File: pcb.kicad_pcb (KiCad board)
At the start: 2 copper layers, 247.4 x 96.5 mm, 228 parts, among them J0 USB_mini_micro_B, P1 CONN_3X2, P2 CONN_4, SW1.1 Backtick, SW1.10 9, SW1.11 0, SW1.12 -, SW1.13 =, SW1.2 1, SW1.3 2, SW1.4 3, SW1.5 4, SW1.6 5, SW1.7 6, SW1.8 7, SW1.9 8, SW2A1 Tab, SW2A10 I, SW2A11 O, SW2A12 P, SW2A13 /, SW2A2 Q, SW2A3 W, SW2A4 E, SW2A5 R, SW2A6 T, SW2A8 Y, SW2A9 U, SW2B1 Tab, SW2B10 I, SW2B11 O, SW2B12 P, SW2B13 /, SW2B2 Q, SW2B3 W, SW2B4 E, SW2B5 R, SW2B6 T, SW2B7 Y, SW2B8 Y, SW2B9 U, SW3A1 Bksp, SW3A10 K, SW3A11 L, SW3A12 ;, SW3A13 Enter, SW3A2 A, SW3A3 S, SW3A4 D, SW3A5 F, SW3A6 G, SW3A8 H, SW3A9 J, SW3B1 Bksp, SW3B10 K, SW3B11 L, SW3B12 ;, SW3B13 Enter, SW3B2 A, SW3B3 S, SW3B4 D, SW3B5 F, SW3B6 G, SW3B7 H, SW3B8 H, SW3B9 J, SW4A1 LShift, SW4A10 ,, SW4A11 ., SW4A13 RShift, SW4A3 Z, SW4A4 X, SW4A5 C, SW4A6 V, SW4A8 N, SW4A9 M, SW4B1 LShift, SW4B10 ,, SW4B11 ., SW4B12 .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

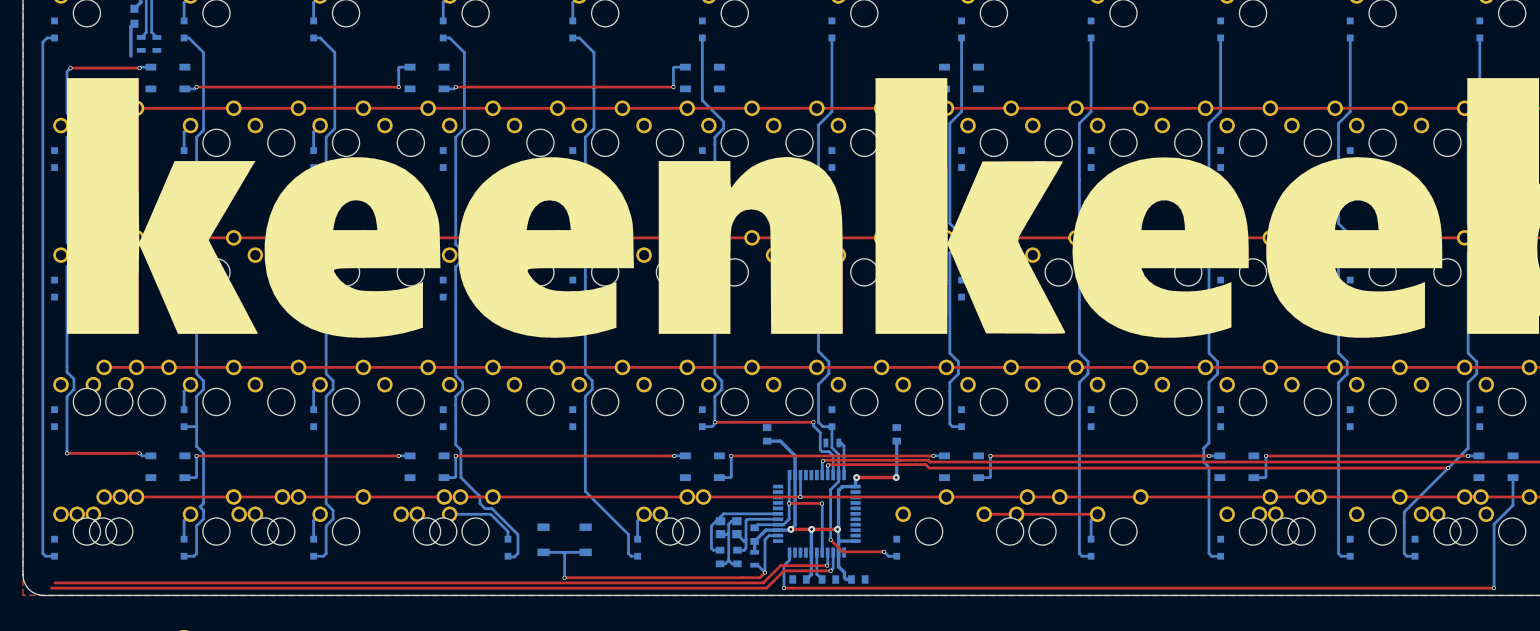
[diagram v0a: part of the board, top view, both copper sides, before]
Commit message: About half of rows/columns connected to microcontroller.
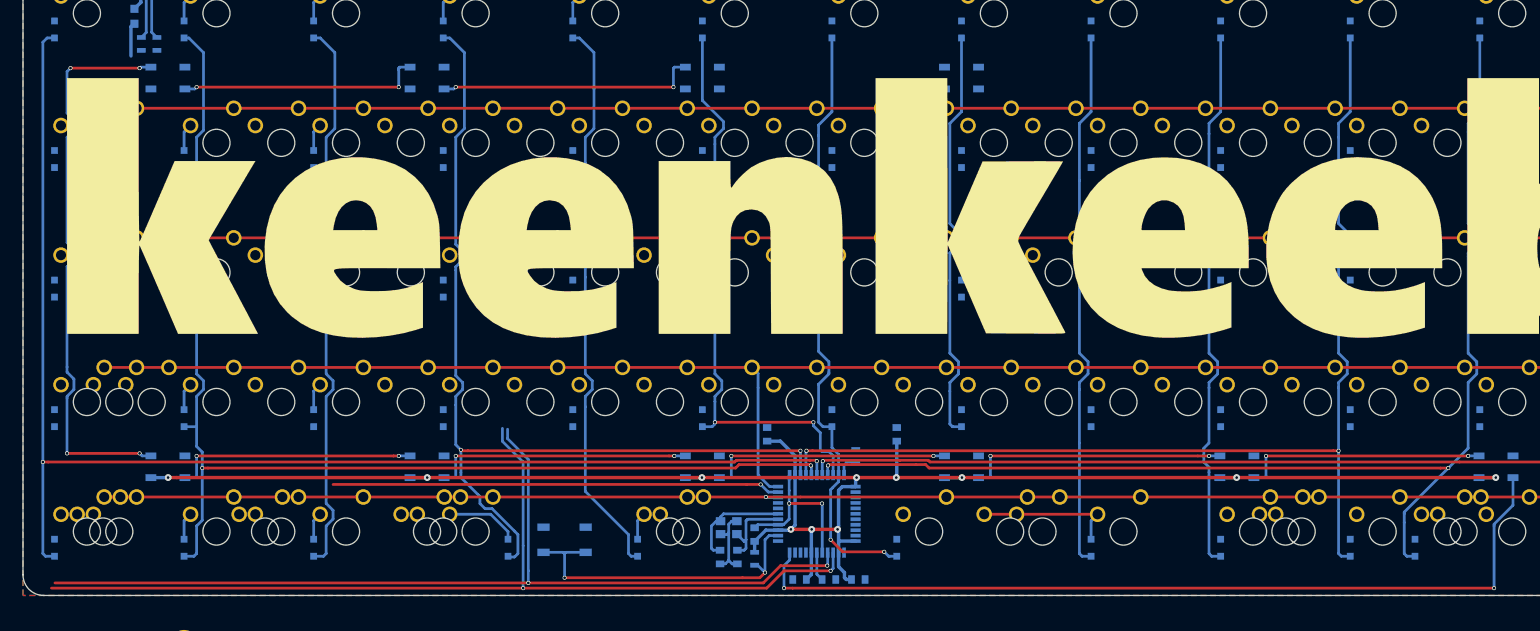
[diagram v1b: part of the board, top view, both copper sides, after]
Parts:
- moved G3 301.4 mm to (321.8, 138.8), turned to 270 degrees
- moved G2 288.6 mm to (319.0, 129.4), turned to 270 degrees
- moved R4 3.92 mm to (198.8, 165.1), turned to 270 degrees
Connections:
- U1 pad 1: /matrix/Col2 -> Net-(U1-Pad1)
- U1 pad 20: Net-(U1-Pad20) -> /matrix/Row5
- U1 pad 21: /matrix/Col11 -> Net-(U1-Pad21)
- U1 pad 22: /matrix/Col9 -> /matrix/Row4
- U1 pad 25: /matrix/Row5 -> /matrix/Col4
- U1 pad 26: Net-(U1-Pad26) -> /matrix/Col11
- U1 pad 27: Net-(U1-Pad27) -> /matrix/Col2
- U1 pad 28: Net-(U1-Pad28) -> /matrix/Col1
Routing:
- net VCC: track 75.7 -> 280.0 mm, vias 5 -> 11
- net /matrix/Col1: track 79.0 -> 195.0 mm, vias 0 -> 2
- net /matrix/Col2: track 88.3 -> 178.9 mm, vias 0 -> 2
- net /matrix/Col11: track 80.5 -> 162.3 mm, vias 0 -> 2
- net Net-(U1-Pad21): track 0.00 -> 65.9 mm, vias 0 -> 1
- net /matrix/Col4: track 86.0 -> 139.5 mm, vias 0 -> 2
- net Net-(R1-Pad1): track 118.4 -> 143.2 mm, vias 1 -> 2
- net Net-(R2-Pad1): track 116.5 -> 140.4 mm, vias 1 -> 2
- net /matrix/Row4: track 228.6 -> 248.4 mm
- net Net-(R4-Pad2): track 5.22 -> 3.35 mm
- net /matrix/Row5: track 231.8 -> 230.4 mm

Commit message: Focusing efforts on one main layout (semi-ortho), so that PCB-mounted and Alps components can be supported
Updated keenkeeb-reb1.png with new layout.
Started removing footprints and adding new spacebar footprints.
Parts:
- removed SW2B1: Tab, footprints:MX_100_Plate
- removed SW2B10: I, footprints:MX_100_Plate
- removed SW2B11: O, footprints:MX_100_Plate
- removed SW2B12: P, footprints:MX_100_Plate
- removed SW2B13: /, footprints:MX_100_Plate
- removed SW2B2: Q, footprints:MX_100_Plate
- removed SW2B3: W, footprints:MX_100_Plate
- removed SW2B4: E, footprints:MX_100_Plate
- removed SW2B5: R, footprints:MX_100_Plate
- removed SW2B6: T, footprints:MX_100_Plate
- removed SW2B7, SW2B8: Y, footprints:MX_100_Plate
- removed SW2B9: U, footprints:MX_100_Plate
- removed SW3B1: Bksp, footprints:MX_100_Plate
- removed SW3B10: K, footprints:MX_100_Plate
- removed SW3B11: L, footprints:MX_100_Plate
- removed SW3B12: ;, footprints:MX_100_Plate
- removed SW3B13: Enter, footprints:MX_100_Plate
- removed SW3B2: A, footprints:MX_100_Plate
- removed SW3B3: S, footprints:MX_100_Plate
- removed SW3B4: D, footprints:MX_100_Plate
- removed SW3B5: F, footprints:MX_100_Plate
- removed SW3B6: G, footprints:MX_100_Plate
- removed SW3B7, SW3B8: H, footprints:MX_100_Plate
- removed SW3B9: J, footprints:MX_100_Plate
- removed SW4B1: LShift, footprints:MX_150_Plate
- removed SW4B10: ,, footprints:MX_100_Plate
- removed SW4B11, SW4B12: ., footprints:MX_100_Plate
- removed SW4B13: RShift, footprints:MX_150_Plate
- removed SW4B2, SW4B3: Z, footprints:MX_100_Plate
- removed SW4B4: X, footprints:MX_100_Plate
- removed SW4B5: C, footprints:MX_100_Plate
- removed SW4B6: V, footprints:MX_100_Plate
- removed SW4B8: N, footprints:MX_100_Plate
- removed SW4B9: M, footprints:MX_100_Plate
- removed SW5B1: LCtrl, footprints:MX_125_Plate
- removed SW5B10, SW5B12, SW5B13: 1.25, footprints:MX_125_Plate
- removed SW5B2: LGUI, footprints:MX_125_Plate
- removed SW5B4: LAlt, footprints:MX_125_Plate
- added LED11: WS2812b, LEDs:LED_WS2812B-PLCC4, B.Cu at (254.8, 109.5)
- added LED12: WS2812b, LEDs:LED_WS2812B-PLCC4, B.Cu at (292.9, 109.5)
- added SW5B7: 2.75, footprints:MX_275_Plate_NoStabHoles, F.Cu at (178.6, 176.2)
- added SW5C9: 1.5, footprints:MX_150_Plate, F.Cu at (233.4, 176.2)
- added SW5D7: 1, footprints:MX_100_Plate, F.Cu at (161.9, 176.2)
- SW5A7: renamed from SW5A5; value Fn -> 2.25
- SW5A9: value Space -> 2.75
- SW5B9: value Space -> 2.25; footprint footprints:MX_275_Plate_NoStabHoles -> footprints:MX_225_Plate_NoStabHoles
- SW5C5: value Fn -> 1.5; footprint footprints:MX_200_Plate_NoStabHoles -> footprints:MX_150_Plate
- SW5C7: value Fn -> 2/3
- moved C1 128.3 mm to (90.2, 109.1), turned to 90 degrees
- moved C8 126.3 mm to (83.1, 128.1), turned to 180 degrees
- moved R3 118.8 mm to (79.2, 124.1)
- moved C7 103.6 mm to (88.4, 126.4), turned to 180 degrees
- moved U1 101.2 mm to (102.4, 128.6), turned to 270 degrees
- moved C5 101.0 mm to (110.0, 122.3)
- moved PB0 99.6 mm to (59.5, 152.4)
- moved C4 98.5 mm to (120.7, 123.8)
- moved C6 84.9 mm to (106.9, 140.8), turned to 270 degrees
- moved OSC0 81.6 mm to (114.0, 127.6), turned to 315 degrees
- moved C2 78.7 mm to (123.7, 126.4), turned to 0 degrees
- moved C3 75.1 mm to (123.7, 128.9), turned to 0 degrees
- moved D2.3 19.2 mm to (138.1, 119.1)
- moved D3.3 19.2 mm to (138.1, 138.1)
- moved D2.2 19.2 mm to (119.1, 119.1)
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- renumbered SW4B7 to SW4.7, SW5C9 to SW5D9
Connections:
- D5.5 pad 2: /matrix/Col5 -> Net-(D5.5-Pad2)
- SW5A4 pad 1: /matrix/Row5 -> Net-(D5.4-Pad1)
- SW5A4 pad 2: Net-(D5.4-Pad1) -> /matrix/Row5
- SW5A7 pad 1: /matrix/Row5 -> Net-(D5.7-Pad1)
- SW5A7 pad 2: Net-(D5.5-Pad1) -> /matrix/Row5
- SW5B9 pad 1: /matrix/Row5 -> Net-(D5.9-Pad1)
- SW5B9 pad 2: Net-(D5.9-Pad1) -> /matrix/Row5
- SW5D9 pad 1: /matrix/Row5 -> Net-(D5.9-Pad1)
- SW5D9 pad 2: Net-(D5.9-Pad1) -> /matrix/Row5
- U1 pad 20: /matrix/Row5 -> /matrix/Col13
- U1 pad 21: Net-(U1-Pad21) -> /matrix/Col12
- U1 pad 22: /matrix/Row4 -> /matrix/Col11
- U1 pad 25: /matrix/Col4 -> /matrix/Col10
- U1 pad 26: /matrix/Col11 -> /matrix/Col9
- U1 pad 27: /matrix/Col2 -> /matrix/Col8
- U1 pad 28: /matrix/Col1 -> /matrix/Col7
- U1 pad 29: /matrix/Col13 -> /matrix/Col6
- U1 pad 30: /matrix/Col12 -> /matrix/Col5
- U1 pad 31: /matrix/Col6 -> /matrix/Col4
- U1 pad 32: /matrix/Col7 -> /matrix/Col3
- U1 pad 36: Net-(U1-Pad36) -> /matrix/Row5
- U1 pad 37: Net-(U1-Pad37) -> /matrix/Row4
- U1 pad 38: Net-(U1-Pad38) -> /matrix/Row3
- U1 pad 39: Net-(U1-Pad39) -> /matrix/Row2
- U1 pad 40: Net-(U1-Pad40) -> /matrix/Row1
- U1 pad 41: Net-(U1-Pad41) -> /matrix/Col1
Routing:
- net /matrix/Row4: track 248.4 -> 0.00 mm
- net /matrix/Row5: track 230.4 -> 0.00 mm, vias 1 -> 0
- net /matrix/Row3: track 228.6 -> 0.00 mm
- net /matrix/Col1: track 195.0 -> 0.00 mm, vias 2 -> 0
- net /matrix/Col13: track 191.8 -> 4.72 mm, vias 2 -> 1
- net /matrix/Col2: track 178.9 -> 0.00 mm, vias 2 -> 0
- net /matrix/Col12: track 177.1 -> 4.99 mm, vias 2 -> 1
- net /matrix/Col11: track 162.3 -> 5.26 mm, vias 2 -> 1
- net Net-(R1-Pad1): track 143.2 -> 0.00 mm, vias 2 -> 0
- net Net-(R2-Pad1): track 140.4 -> 0.00 mm, vias 2 -> 0
- net /matrix/Col4: track 139.5 -> 0.00 mm, vias 2 -> 0
- net /underglow/Din: track 127.4 -> 0.00 mm, vias 2 -> 0
- net /matrix/Col7: track 90.3 -> 0.00 mm, vias 2 -> 0
- net /matrix/Col6: track 86.3 -> 0.00 mm, vias 2 -> 0
- net /matrix/Col5: track 84.0 -> 0.00 mm
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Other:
- board text added: "3"
- board text removed: "1.25"

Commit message: Started to layout with MX/Alps footprints
Added footprints that support Cherry MX and Alps switches.
Started to layout the board with new footprints.  Will support PCB
mounted switches/stabs.
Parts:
- removed D2.7, D3.7: D, Diodes_SMD:D_SOD-323_HandSoldering
- removed SW5D7: 1, footprints:MX_100_Plate
- added >NAME: >VALUE, footprints:Mx_Alps_100, F.Cu at (202.4, 223.8)
- added SW5D5: 1, footprints:Mx_Alps_100, F.Cu at (161.9, 176.2)
- SW1.1, SW1.10, SW1.11, SW1.12, SW1.13, SW1.2, SW1.3, SW1.4, SW1.5, SW1.6, SW1.7, SW1.8, SW1.9, SW2A10, SW2A11, SW2A12, SW2A2, SW2A3, SW2A4, SW2A5, SW2A6, SW2A8, SW2A9, SW3A10, SW3A11, SW3A12, SW3A2, SW3A3, SW3A4, SW3A5, SW3A6, SW3A8, SW3A9, SW4.7, SW4A10, SW4A11, SW4A3, SW4A4, SW4A5, SW4A6, SW4A8, SW4A9, SW4C1, SW4C12, SW4C13, SW4C2, SW5A12, SW5A2, SW5C1, SW5C10, SW5C11, SW5C12, SW5C13, SW5C2, SW5C3, SW5C4, SW5D9: footprint footprints:MX_100_Plate -> footprints:Mx_Alps_100
- SW2A1, SW2A13, SW3A1, SW3A13, SW5A10, SW5A13, SW5A4, SW5C5, SW5C9: footprint footprints:MX_150_Plate -> footprints:Mx_Alps_150
- SW4A1, SW4A13, SW5C7: footprint footprints:MX_200_Plate_NoStabHoles -> footprints:Mx_Alps_200
- SW5A1: value LCtrl -> 1.5; footprint footprints:MX_150_Plate -> footprints:Mx_Alps_150
- SW5A7, SW5B9: footprint footprints:MX_225_Plate_NoStabHoles -> footprints:Mx_Alps_225
- SW5A9, SW5B7: footprint footprints:MX_275_Plate_NoStabHoles -> footprints:Mx_Alps_275
- moved LED6 212.6 mm to (302.4, 109.5), turned to 180 degrees
- moved LED7 212.6 mm to (302.4, 166.7), turned to 0 degrees
- moved LED1 203.5 mm to (97.6, 109.5), turned to 180 degrees
- moved LED12 203.5 mm to (97.6, 166.7), turned to 0 degrees
- moved Hole3 170.8 mm to (200.0, 138.1)
- moved LED5 138.5 mm to (261.9, 109.5), turned to 180 degrees
- moved LED8 138.5 mm to (261.9, 166.7), turned to 0 degrees
- moved LED11 129.9 mm to (138.1, 166.7), turned to 0 degrees
- moved LED2 129.9 mm to (138.1, 109.5), turned to 180 degrees
- moved R4 103.5 mm to (97.6, 142.9), turned to 90 degrees
- moved LED4 72.9 mm to (221.5, 109.5), turned to 180 degrees
- moved LED9 72.9 mm to (221.5, 166.7), turned to 0 degrees
- moved LED10 67.4 mm to (178.6, 166.7), turned to 0 degrees
- moved LED3 67.4 mm to (178.6, 109.5), turned to 180 degrees
- moved PB0 39.6 mm to (81.0, 119.1), turned to 270 degrees
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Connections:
- P1 pad 1: /underglow/Din -> /microcontroller/MISO
- SW5A1 pad 1: /matrix/Row5 -> Net-(D5.1-Pad1)
- SW5A1 pad 2: Net-(D5.1-Pad1) -> /matrix/Row5
- SW5A10 pad 1: /matrix/Row5 -> Net-(D5.10-Pad1)
- SW5A10 pad 2: Net-(D5.10-Pad1) -> /matrix/Row5
- SW5A4 pad 1: Net-(D5.4-Pad1) -> /matrix/Row5
- SW5A4 pad 2: /matrix/Row5 -> Net-(D5.4-Pad1)
- SW5A7 pad 1: Net-(D5.7-Pad1) -> /matrix/Row5
- SW5A7 pad 2: /matrix/Row5 -> Net-(D5.7-Pad1)
- SW5A9 pad 1: /matrix/Row5 -> Net-(D5.9-Pad1)
- SW5A9 pad 2: Net-(D5.9-Pad1) -> /matrix/Row5
- SW5B7 pad 1: /matrix/Row5 -> Net-(D5.7-Pad1)
- SW5B7 pad 2: Net-(D5.7-Pad1) -> /matrix/Row5
- SW5B9 pad 1: Net-(D5.9-Pad1) -> /matrix/Row5
- SW5B9 pad 2: /matrix/Row5 -> Net-(D5.9-Pad1)
- SW5C13 pad 1: /matrix/Row5 -> Net-(D5.13-Pad1)
- SW5C13 pad 2: Net-(D5.13-Pad1) -> /matrix/Row5
- SW5C4 pad 1: /matrix/Row5 -> Net-(D5.4-Pad1)
- SW5C4 pad 2: Net-(D5.4-Pad1) -> /matrix/Row5
- SW5C5 pad 1: /matrix/Row5 -> Net-(D5.5-Pad1)
- SW5C5 pad 2: Net-(D5.5-Pad1) -> /matrix/Row5
- SW5C9 pad 1: /matrix/Row5 -> Net-(D5.9-Pad1)
- SW5C9 pad 2: Net-(D5.9-Pad1) -> /matrix/Row5
- SW5D9 pad 1: Net-(D5.9-Pad1) -> /matrix/Row5
- SW5D9 pad 2: /matrix/Row5 -> Net-(D5.9-Pad1)
- U1 pad 1: Net-(U1-Pad1) -> /underglow/Din
- U1 pad 11: /underglow/Din -> /microcontroller/MISO
- U1 pad 12: /microcontroller/LED -> /matrix/Col2
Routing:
- net VCC: track 243.7 -> 538.9 mm, vias 6 -> 15
- net /matrix/Row5: track 0.00 -> 270.5 mm
- net /matrix/Row4: track 0.00 -> 236.3 mm
- net /matrix/Row3: track 0.00 -> 225.8 mm
- net /matrix/Col13: track 4.72 -> 203.4 mm
- net /matrix/Col12: track 4.99 -> 180.3 mm
- net /matrix/Col11: track 5.26 -> 161.3 mm
- net /matrix/Col10: track 0.00 -> 147.8 mm, vias 0 -> 1
- net /matrix/Col3: track 0.00 -> 147.4 mm, vias 0 -> 2
- net /matrix/Col9: track 0.00 -> 128.3 mm, vias 0 -> 1
- net /matrix/Col8: track 0.00 -> 116.9 mm, vias 0 -> 1
- net /matrix/Col2: track 0.00 -> 116.5 mm
- net /matrix/Col7: track 0.00 -> 108.8 mm, vias 0 -> 1
- net /matrix/Col6: track 0.00 -> 100.6 mm, vias 0 -> 1
- net /matrix/Col1: track 0.00 -> 98.9 mm
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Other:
- board size 247.4 x 96.5 mm -> 247.4 x 97.8 mm
- board text added: "Moved switch diodes 0.1588 in left"

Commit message: Connected most of the components on the board
TODO:
Replace P1 with 1x6 header for SPI, Vcc, GND
Add test pads
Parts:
- removed >NAME: >VALUE, footprints:Mx_Alps_100
- removed D1: LED, footprints:LED_3mm_plusminus
- removed R5: 100, Resistors_SMD:R_0805
- added C19: 0.1u, Capacitors_SMD:C_0805, B.Cu at (131.0, 166.7)
- added C20: 0.1u, Capacitors_SMD:C_0805, B.Cu at (97.6, 171.4)
- added P3: CONN_01X03, Pin_Headers:Pin_Header_Straight_1x03_Pitch2.54mm, B.Cu at (81.2, 120.5)
- added Stitch1: Via-0.6mm, footprints:Via-0.6mm, F.Cu at (95.6, 121.2)
- added Stitch2: Via-0.6mm, footprints:Via-0.6mm, F.Cu at (195.6, 121.2)
- added Stitch3: Via-0.6mm, footprints:Via-0.6mm, F.Cu at (84.2, 129.9)
- P1: value CONN_3X2 -> CONN_02X03; moved to F.Cu
- P2: value CONN_4 -> CONN_01X04
- moved C14 299.7 mm to (309.6, 109.5), turned to 90 degrees
- moved C13 275.8 mm to (269.1, 109.5), turned to 90 degrees
- moved C15 263.6 mm to (301.8, 171.4), turned to 90 degrees
- moved C12 254.5 mm to (228.6, 109.5), turned to 90 degrees
- moved C16 218.5 mm to (254.8, 166.7), turned to 270 degrees
- moved C11 205.8 mm to (185.7, 109.5), turned to 90 degrees
- moved C17 186.0 mm to (213.4, 165.1)
- moved C10 169.3 mm to (145.3, 109.5), turned to 90 degrees
- moved C18 161.3 mm to (171.4, 166.7), turned to 270 degrees
- moved C9 159.3 mm to (104.6, 109.5)
- moved P1 107.4 mm to (132.1, 93.6)
- moved PB0 60.5 mm to (140.7, 128.6), turned to 0 degrees
- moved P2 52.9 mm to (81.2, 134.9)
- moved R3 38.8 mm to (124.8, 123.3), turned to 270 degrees
- moved Hole1 36.3 mm to (81.0, 109.5)
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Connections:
- D5.5 pad 2: Net-(D5.5-Pad2) -> /matrix/Col5
- LED11 pad 2: Net-(LED10-Pad2) -> Net-(LED11-Pad2)
- LED11 pad 4: Net-(LED10-Pad4) -> Net-(LED10-Pad2)
- LED12 pad 2: Net-(LED10-Pad2) -> Net-(LED12-Pad2)
- LED12 pad 4: Net-(LED10-Pad4) -> Net-(LED11-Pad2)
- P2 pad 2: /microcontroller/SDA -> VCC
- P2 pad 3: VCC -> /microcontroller/SDA
- U1 pad 36: /matrix/Row5 -> /matrix/Col1
- U1 pad 37: /matrix/Row4 -> /matrix/Row3
- U1 pad 38: /matrix/Row3 -> /matrix/Row4
- U1 pad 39: /matrix/Row2 -> /matrix/Row5
- U1 pad 41: /matrix/Col1 -> /matrix/Row2
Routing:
- net VCC: track 538.9 -> 682.6 mm, vias 15 -> 20
- net /matrix/Col9: track 128.3 -> 248.5 mm, vias 1 -> 2
- net /matrix/Col11: track 161.3 -> 275.4 mm, vias 1 -> 2
- net /matrix/Col5: track 83.6 -> 194.8 mm, vias 1 -> 2
- net /matrix/Col12: track 180.3 -> 289.5 mm, vias 1 -> 2
- net /matrix/Col10: track 147.8 -> 255.9 mm, vias 1 -> 2
- net /matrix/Col4: track 65.9 -> 167.1 mm, vias 1 -> 2
- net /matrix/Col13: track 203.4 -> 303.7 mm, vias 1 -> 2
- net /matrix/Col7: track 108.8 -> 197.3 mm, vias 1 -> 2
- net /matrix/Col8: track 116.9 -> 199.5 mm, vias 1 -> 2
- net /matrix/Col6: track 100.6 -> 180.4 mm, vias 1 -> 2
- net Net-(LED6-Pad2): track 0.00 -> 62.7 mm
- net /matrix/Row5: track 270.5 -> 332.6 mm, vias 0 -> 2
- net /matrix/Row1: track 237.1 -> 278.9 mm, vias 0 -> 2
- net Net-(LED11-Pad2): track 0.00 -> 40.0 mm, vias 0 -> 2
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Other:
- board text added: "PE6"

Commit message: More progress on PCB
Cleaned up silkscreen layers
Updated switch footprints to remove front layer and hide reference on
back layer
Moved references on back layer
Moved bottom mounting holes on PCB
Cleaned up matrix schematic
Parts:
- added P4: CONN_01X02, Pin_Headers:Pin_Header_Straight_1x02_Pitch2.54mm, B.Cu at (142.6, 118.2)
- added Stitch4: Via-0.6mm, footprints:Via-0.6mm, F.Cu at (228.7, 168.0)
- added Stitch4: Via-0.6mm, footprints:Via-0.6mm, F.Cu at (172.8, 169.7)
- added Stitch4: Via-0.6mm, footprints:Via-0.6mm, F.Cu at (193.9, 169.2)
- P1: value CONN_02X03 -> CONN_01X06; footprint Pin_Headers:Pin_Header_Straight_2x03_Pitch2.54mm -> Pin_Headers:Pin_Header_Straight_1x06_Pitch2.54mm; moved to B.Cu
- moved Hole4 54.8 mm to (152.4, 183.4)
- moved Hole5 54.8 mm to (247.7, 183.4)
- moved P1 17.8 mm to (114.3, 93.6), turned to 180 degrees
- moved Stitch2 11.2 mm to (185.3, 125.5)
- moved Stitch1 3.68 mm to (96.9, 117.7)
- renumbered SW2A1 to SW2.1, SW2A10 to SW2.10, SW2A11 to SW2.11, SW2A12 to SW2.12, SW2A13 to SW2.13, SW2A2 to SW2.2, SW2A3 to SW2.3, SW2A4 to SW2.4, SW2A5 to SW2.5, SW2A6 to SW2.6, SW2A8 to SW2.8, SW2A9 to SW2.9, SW3A1 to SW3.1, SW3A10 to SW3.10, SW3A11 to SW3.11, SW3A12 to SW3.12, SW3A13 to SW3.13, SW3A2 to SW3.2, SW3A3 to SW3.3, SW3A4 to SW3.4, SW3A5 to SW3.5, SW3A6 to SW3.6, SW3A8 to SW3.8, SW3A9 to SW3.9, SW4A10 to SW4.10, SW4A11 to SW4.11, SW4C12 to SW4.12, SW4C2 to SW4.2, SW4A3 to SW4.3, SW4A4 to SW4.4, SW4A5 to SW4.5, SW4A6 to SW4.6, SW4A8 to SW4.8, SW4A9 to SW4.9, SW4C1 to SW4B1, SW4C13 to SW4B13, SW5C1 to SW5B1, SW5C10 to SW5B10, SW5C11 to SW5B11, SW5C12 to SW5B12, SW5C13 to SW5B13, SW5C2 to SW5B2, SW5C3 to SW5B3, SW5C4 to SW5B4
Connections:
- P1 pad 1: /microcontroller/MISO -> GND
- P1 pad 3: /microcontroller/SCK -> /microcontroller/MISO
- P1 pad 5: /microcontroller/nRST -> /microcontroller/SCK
- P1 pad 6: GND -> /microcontroller/SS
- U1 pad 8: Net-(U1-Pad8) -> /microcontroller/SS
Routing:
- net /microcontroller/SS: track 0.00 -> 25.5 mm, vias 0 -> 1
- net Net-(U1-Pad8): track 16.5 -> 0.00 mm
- net /microcontroller/MOSI: track 15.4 -> 31.7 mm, vias 0 -> 2
- net /microcontroller/MISO: track 14.9 -> 30.4 mm, vias 0 -> 2
- net VCC: track 682.6 -> 698.0 mm, vias 20 -> 21
- net /microcontroller/SCK: track 16.0 -> 26.4 mm, vias 0 -> 2
- net /microcontroller/nRST: track 40.6 -> 46.6 mm
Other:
- board text added: "10"
- board text added: "11"
- board text added: "12"
- board text added: "13"
- board text added: "4"
- board text added: "5"
- board text added: "6"
- board text added: "7"
- board text added: "8"
- board text added: "9"
- board text added: "RST"
- board text added: "SCK"
- board text added: "SI"
- board text added: "SO"
- board text added: "SS"

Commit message: Added new graphic for back side of PCB
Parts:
- removed G2: LOGO, graphics:keenkeeb-graphic-small
- removed G3: LOGO, graphics:rev0-graphic
- added G***: LOGO, graphics:keenkeeb-rev1-graphic, B.Cu at (306.1, 129.5)
